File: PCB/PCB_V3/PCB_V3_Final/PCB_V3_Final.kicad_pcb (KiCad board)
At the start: 2 copper layers, 84 parts, among them J1 ESP_Left, J10 LHS_Arrow_+ve, J11 MCP_B0, J12 LHS_Arrow_-ve, J13 ACS2_Screw, J14 ACS4_Screw, J15 LAN8720_pins_2, J16 LAN8720_pins_1, J17 MCP_VCC_LINE, J18 RHS_Arrow_+ve, J19 RHS_Arrow_-ve, J2 ESP_Right, J20 AMS_IP_Pins, J21 BC1_IN+, J22 BC1_IN-, J23 BC3_IN+, J24 BC3_IN-, J25 AMS_OP_Pins, J26 BC1_OUT+, J27 BC1_OUT-, J28 BC3_OUT+, J29 BC3_OUT-, J3 ACS1_Pins, J30 STATIC_LED_1, J31 STATIC_LED_2, J32 BC2_IN+, J33 BC2_IN-, J34 BC5_IN+, J35 BC5_IN-, J36 I/P_Terminal, J37 Battery_Terminal, J38 BC2_OUT+, J39 BC2_OUT-, J4 ACS3_Pins, J40 BC5_OUT+, J41 BC5_OUT-, J5 ACS3_Screw, J6 ACS1_Screw, J7 ACS2_pins, J8 MCP_A0, J9 ACS4_Pins, Q1 IRLZ44N, Q10 IRLZ44N, Q2 IRLZ44N, Q3 IRLZ44N, Q4 IRLZ44N, Q5 IRLZ44N, Q6 IRLZ44N, Q7 IRLZ44N, Q8 IRLZ44N, Q9 IRLZ44N

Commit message: Uploading the final PCB files
1. Finished product
2. Made the remaining connections
3. Added the mounting holes for the PCB
4. Final producct --> has to be reviewed in the meeting
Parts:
- added H1: MountingScrew, MountingHole:MountingHole_3.2mm_M3, F.Cu at (219.8, 25.2)
- added H2: MountingScrew, MountingHole:MountingHole_3.2mm_M3, F.Cu at (74.5, 25.2)
- added H3: MountingScrew, MountingHole:MountingHole_3.2mm_M3, F.Cu at (75.5, 154.0)
- added H4: MountingScrew, MountingHole:MountingHole_3.2mm_M3, F.Cu at (219.2, 154.0)
- moved R23 98.9 mm to (92.2, 147.9)
- moved R24 96.5 mm to (102.3, 151.5), turned to 180 degrees
- moved Q10 41.0 mm to (130.3, 108.5)
- moved R15 41.0 mm to (135.8, 106.5)
- moved R20 41.0 mm to (145.9, 110.0)
- moved Q6 32.0 mm to (130.0, 143.5)
- moved R11 32.0 mm to (135.9, 143.5)
- moved R16 32.0 mm to (146.1, 147.0)
- moved Q9 22.5 mm to (130.0, 117.5)
- moved R14 22.5 mm to (135.4, 116.0)
- moved R19 22.5 mm to (145.6, 119.5)
- moved R26 15.9 mm to (131.5, 51.0), turned to 180 degrees
- moved Q7 14.0 mm to (129.8, 135.0)
- moved R12 14.0 mm to (135.8, 134.5)
- moved R17 14.0 mm to (145.9, 138.0)
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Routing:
- net /5V: track 0.00 -> 303.5 mm, vias 0 -> 2
- net /12V_LR: track 0.00 -> 295.6 mm, vias 0 -> 2
- net /LHS_LED_IP+: track 0.00 -> 259.6 mm
- net /RHS_LED_IP+: track 0.00 -> 256.6 mm
- net /D35: track 0.00 -> 169.7 mm, vias 0 -> 1
- net /D34: track 0.00 -> 162.4 mm
- net /D32: track 0.00 -> 155.0 mm
- net /BATT_VD: track 0.00 -> 137.5 mm, vias 0 -> 6
- net /D33: track 0.00 -> 133.4 mm
- net /14.5: track 15.1 -> 138.9 mm
- net /LHS_LED_1: track 0.00 -> 109.3 mm
- net /D13: track 12.6 -> 112.3 mm, vias 0 -> 4
- net /LHS_LED_2: track 0.00 -> 99.1 mm
- net /B0: track 0.00 -> 91.1 mm
- net /LHS_LED_3: track 0.00 -> 85.6 mm
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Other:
- board outline added: 152.5 x 136.2 mm
- board text added: "12V"
- board text added: "5V"
- board text added: "ACS712"
- board text added: "Battery_Terminal"
- board text added: "I/P_Terminal"
- board text added: "IN+"
- board text added: "LAN PORT HERE"
- board text added: "LHS_+ve"
- board text added: "LHS_-ve"
- board text added: "RHS_+ve"
- board text added: "RHS_-ve"
- board text added: "SCL"
- board text added: "SDA"
- board text added: "Static_LED_1"
- board text added: "Static_LED_2"
- board text added: "TOP"
- board text added: "VCC"
- board text added: "VOUT"

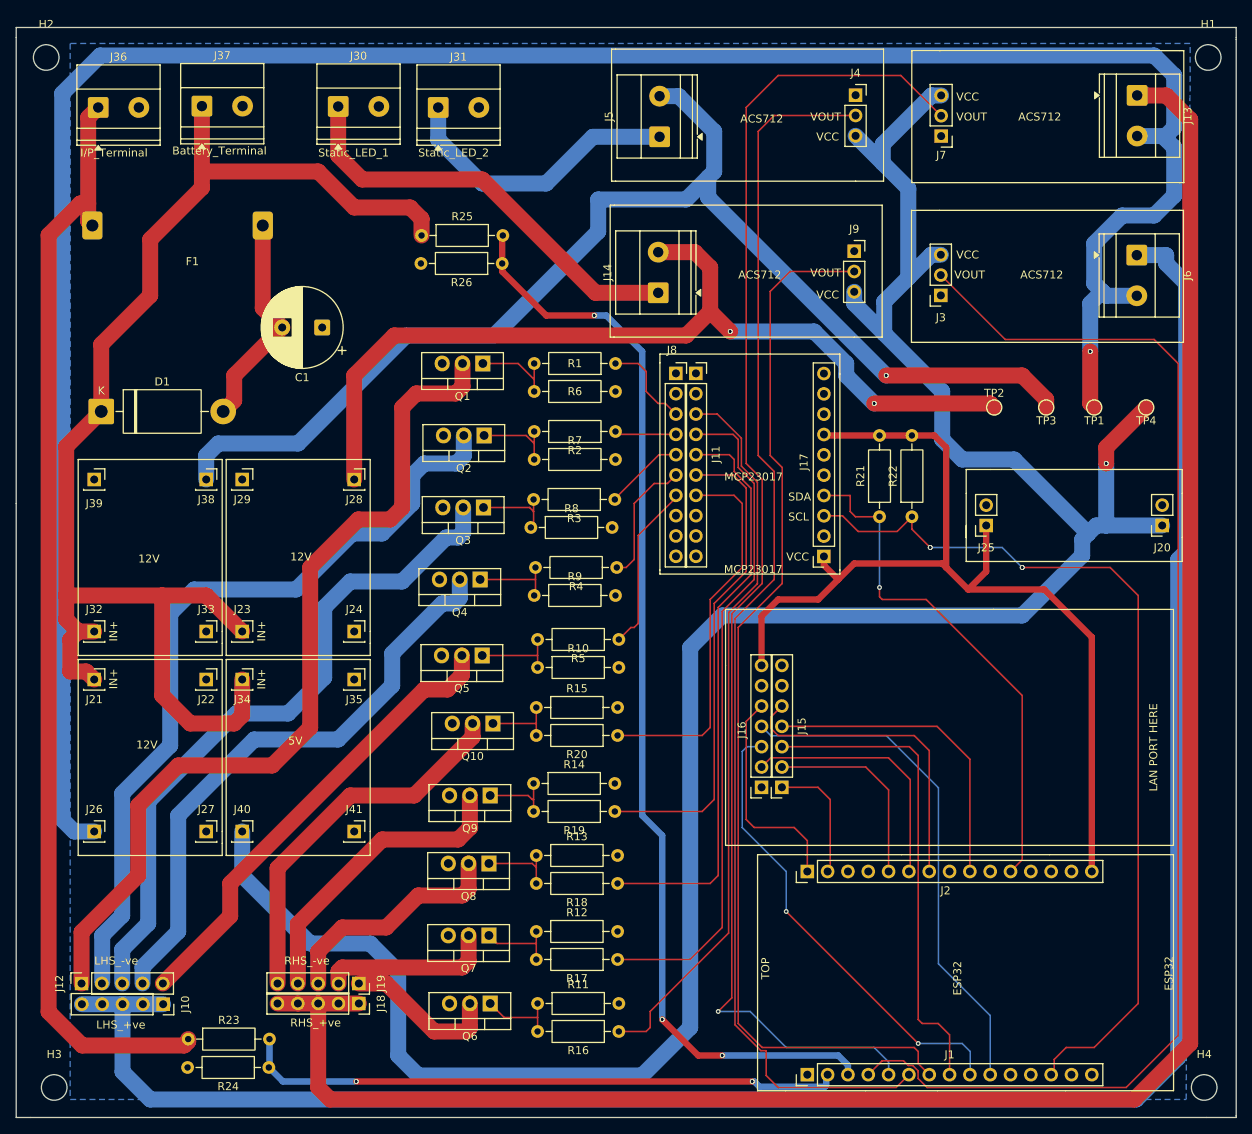
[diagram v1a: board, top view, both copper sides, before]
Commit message: Created and finished coding the firmware_test.ino file
1. Added a README file in the testing folder, that shows all the details of the hardware and software fucntionality
2. Created a test code for testing hardware first
3. Adding a testing criteria document for details of what is getting tested and how to test teh hardware using this code
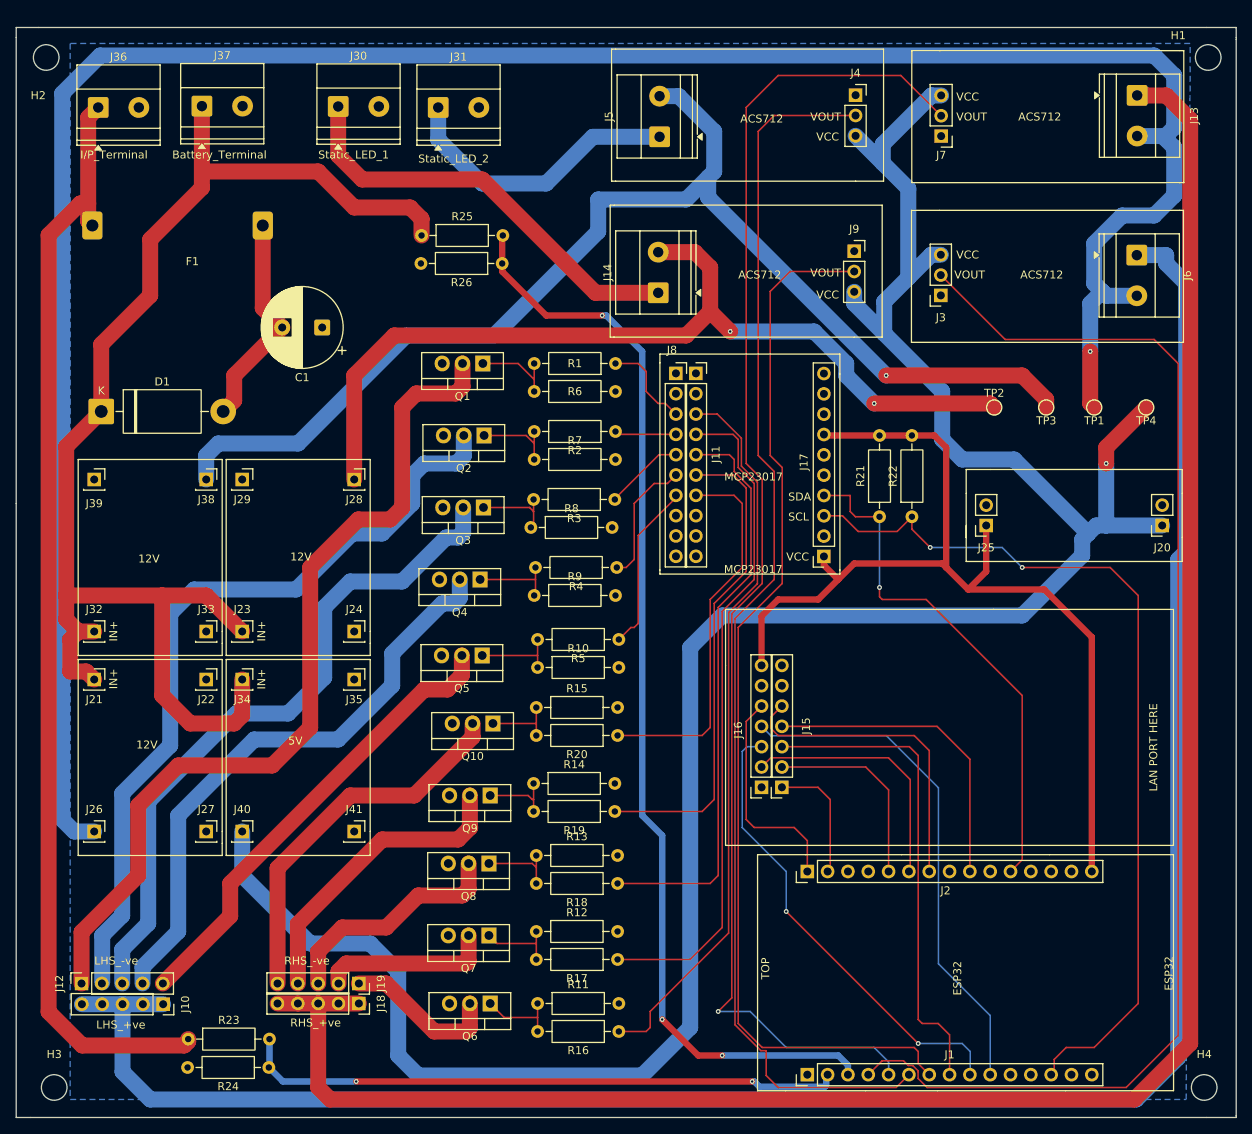
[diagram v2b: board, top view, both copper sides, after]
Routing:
- net /BATT_VD: vias 6 -> 3
- net /PSU_VD: vias 4 -> 2
- net /D13: vias 4 -> 2
- net /5V: vias 2 -> 1
- net /12V_STATIC2: vias 4 -> 2
- net /12V_STATIC1: vias 2 -> 1
- net /12V_LR: vias 2 -> 1
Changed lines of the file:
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@@
 		(tags "Through hole socket strip THT 1x07 2.54mm single row")
 		(property "Reference" "J16"
-			(at 2.46 7.16 90)
+			(at 2.92 7.16 90)
 			(layer "F.SilkS")
 			(effects
@@
 		(tags "mountinghole M3")
 		(property "Reference" "H1"
-			(at 0 -4.15 0)
+			(at -3.75 -2.75 0)
 			(layer "F.SilkS")
 			(effects
@@
 		(tags "Through hole socket strip THT 1x07 2.54mm single row")
 		(property "Reference" "J15"
-			(at -2.5 7.66 90)
+			(at -3.04 7.66 90)
 			(layer "F.SilkS")
 			(effects
@@
 		(tags "mountinghole M3")
 		(property "Reference" "H2"
-			(at 0 -4.15 0)
+			(at -1 4.75 0)
 			(layer "F.SilkS")
 			(effects
@@
 		(tags "THT Terminal Block Phoenix MKDS-1,5-2-5.08 pitch 5.08mm size 10.2x9.8mm drill 1.3mm pad 2.6mm")
 		(property "Reference" "J13"
-			(at 2.54 -6.32 90)
+			(at 2.54 -7.130715 90)
 			(layer "F.SilkS")
 			(effects
@@
 	)
 	(gr_text "I/P_Terminal\n"
-		(at 78.75 37.75 0)
+		(at 78.75 38 0)
 		(layer "F.SilkS")
 		(effects
@@
 	)
 	(gr_text "Battery_Terminal\n"
-		(at 90.25 37.5 0)
+		(at 90.25 38 0)
 		(layer "F.SilkS")
 		(effects
@@
 	)
 	(gr_text "Static_LED_1"
-		(at 108.5 37.75 0)
+		(at 108.5 38 0)
 		(layer "F.SilkS")
 		(effects
@@
 	)
 	(gr_text "Static_LED_2"
-		(at 121 37.75 0)
+		(at 121 38.5 0)
 		(layer "F.SilkS")
 		(effects
@@
 	(segment
 		(start 111.04 139.46)
-		(end 111.5 139)
+		(end 112 138.5)
 		(width 2)
 		(layer "F.Cu")
@@
 	)
 	(segment
-		(start 127.3 138.2)
-		(end 127.3 135)
+		(start 111.04 141)
+		(end 111.04 139.46)
 		(width 2)
 		(layer "F.Cu")
@@
 	)
 	(segment
-		(start 126.5 139)
-		(end 127.3 138.2)
+		(start 127.3 138.2)
+		(end 127.3 135)
 		(width 2)
 		(layer "F.Cu")
@@
 	)
 	(segment
-		(start 111.5 139)
-		(end 126.5 139)
+		(start 127 138.5)
+		(end 127.3 138.2)
 		(width 2)
 		(layer "F.Cu")
@@
 	)
 	(segment
-		(start 111.04 141)
-		(end 111.04 139.46)
+		(start 112 138.5)
+		(end 127 138.5)
 		(width 2)
 		(layer "F.Cu")
@@
 	)
 	(via
-		(at 160 59.5)
-		(size 0.6)
-		(drill 0.3)
-		(layers "F.Cu" "B.Cu")
-		(net "/12V_STATIC2")
-	)
-	(via
-		(at 178 68.5)
-		(size 0.6)
-		(drill 0.3)
-		(layers "F.Cu" "B.Cu")
-		(net "/12V_STATIC2")
-	)
-	(via
 		(at 178 68.5)
 		(size 0.6)
@@
 		(net "/PSU_VD")
 	)
-	(via
-		(at 113.25 153.25)
-		(size 0.6)
-		(drill 0.3)
-		(layers "F.Cu" "B.Cu")
-		(net "/PSU_VD")
-	)
-	(via
-		(at 162.75 153.25)
-		(size 0.6)
-		(drill 0.3)
-		(layers "F.Cu" "B.Cu")
-		(net "/PSU_VD")
-	)
 	(segment
 		(start 163 153.25)
@@
 	)
 	(segment
-		(start 131.5 51)
-		(end 131.5 52)
-		(width 0.8)
+		(start 131.5 47.58)
+		(end 131.58 47.5)
+		(width 0.2)
 		(layer "F.Cu")
 		(net "/BATT_VD")
 	)
 	(segment
-		(start 137 57.5)
-		(end 143 57.5)
+		(start 144 57.5)
+		(end 137 57.5)
 		(width 0.8)
 		(layer "F.Cu")
@@
 	)
 	(segment
-		(start 131.5 47.58)
-		(end 131.58 47.5)
-		(width 0.2)
+		(start 131.5 52)
+		(end 131.5 51)
+		(width 0.8)
 		(layer "F.Cu")
 		(net "/BATT_VD")
@@
 	)
 	(segment
-		(start 131.5 52)
-		(end 137 57.5)
+		(start 131.5 51)
+		(end 131.5 47.58)
 		(width 0.8)
 		(layer "F.Cu")
@@
 	)
 	(segment
-		(start 131.5 51)
-		(end 131.5 47.58)
+		(start 137 57.5)
+		(end 131.5 52)
 		(width 0.8)
 		(layer "F.Cu")
@@
 	)
 	(via
-		(at 143 57.5)
-		(size 0.6)
-		(drill 0.3)
-		(layers "F.Cu" "B.Cu")
-		(net "/BATT_VD")
-	)
-	(via
-		(at 143 57.5)
+		(at 144 57.5)
 		(size 0.6)
 		(drill 0.3)
@@
 		(net "/BATT_VD")
 	)
-	(via
-		(at 159 150)
-		(size 0.6)
-		(drill 0.3)
-		(layers "F.Cu" "B.Cu")
+	(segment
+		(start 149 62)
+		(end 149 120)
+		(width 0.8)
+		(layer "B.Cu")
 		(net "/BATT_VD")
 	)
-	(via
-		(at 151.5 145.5)
-		(size 0.6)
-		(drill 0.3)
-		(layers "F.Cu" "B.Cu")
+	(segment
+		(start 144 57.5)
+		(end 144.5 57.5)
+		(width 0.8)
+		(layer "B.Cu")
 		(net "/BATT_VD")
 	)
@@
 	)
 	(segment
-		(start 143 57.5)
-		(end 144.5 57.5)
-		(width 0.8)
-		(layer "B.Cu")
-		(net "/BATT_VD")
-	)
-	(segment
 		(start 173.5 150)
 		(end 174.72 151.22)
@@
 	)
 	(segment
-		(start 144.5 57.5)
-		(end 149 62)
-		(width 0.8)
-		(layer "B.Cu")
-		(net "/BATT_VD")
-	)
-	(segment
 		(start 174.72 151.22)
 		(end 174.72 152.4)
@@
 	)
 	(segment
-		(start 149 62)
-		(end 149 120)
+		(start 144.5 57.5)
+		(end 149 62)
 		(width 0.8)
 		(layer "B.Cu")
@@
 		(net "/D13")
 	)
-	(via
-		(at 185 86.5)
-		(size 0.6)
-		(drill 0.3)
-		(layers "F.Cu" "B.Cu")
-		(net "/D13")
-	)
-	(via
-		(at 196.5 89)
-		(size 0.6)
-		(drill 0.3)
-		(layers "F.Cu" "B.Cu")
-		(net "/D13")
-	)
 	(segment
 		(start 185 86.5)
@@
 		(net "/12V_STATIC1")
 	)
-	(via
-		(at 179.5 65)
-		(size 0.6)
-		(drill 0.3)
-		(layers "F.Cu" "B.Cu")
-		(net "/12V_STATIC1")
-	)
 	(segment
 		(start 158 34.5)
@@
 		(net "/12V_LR")
 	)
-	(via
-		(at 205 62)
-		(size 0.6)
-		(drill 0.3)
-		(layers "F.Cu" "B.Cu")
-		(net "/12V_LR")
-	)
 	(segment
 		(start 215.5 42.5)
@@
 		(net "/5V")
 	)
-	(via
-		(at 207 76)
-		(size 0.6)
-		(drill 0.3)
-		(layers "F.Cu" "B.Cu")
-		(net "/5V")
-	)
 	(segment
 		(start 99 127.5)
@@
 	)
 	(segment
-		(start 158.5 94)
-		(end 158.5 127.5)
+		(start 162.6 79.1)
+		(end 162.6 89.9)
 		(width 0.2)
 		(layer "F.Cu")
@@
 	)
 	(segment
+		(start 158.5 94)
+		(end 158.5 127.5)
+		(width 0.2)
+		(layer "F.Cu")
+		(net "/B2")
+	)
+	(segment
 		(start 158.5 127.5)
 		(end 157.5 128.5)
@@
 	)
 	(segment
-		(start 157.5 128.5)
-		(end 145.92 128.5)
+		(start 155.714285 74.900001)
+		(end 159.900001 74.900001)
 		(width 0.2)
 		(layer "F.Cu")
@@
 	)
 	(segment
-		(start 160.5 75.5)
-		(end 160.5 77)
+		(start 157.5 128.5)
+		(end 145.92 128.5)
 		(width 0.2)
 		(layer "F.Cu")
@@
 	)
 	(segment
-		(start 155.714285 74.900001)
-		(end 159.900001 74.900001)
-		(width 0.2)
-		(layer "F.Cu")
-		(net "/B2")
-	)
-	(segment
-		(start 162.6 79.1)
-		(end 162.6 89.9)
+		(start 160.5 75.5)
+		(end 160.5 77)
 		(width 0.2)
 		(layer "F.Cu")

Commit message: Final PCB Upload
1. Made all the changes
2. final PCB files and the gerber files uploaded
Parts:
- D1: value 1N5822 -> D_Schottky; footprint Diode_THT:D_DO-201AD_P15.24mm_Horizontal -> Package_TO_SOT_THT:TO-220-2_Vertical
- J28: value BC3_OUT+ -> BC3_IN-
- moved D1 8.77 mm to (89.9, 67.5)
- moved C1 5.00 mm to (104.0, 59.0), turned to 0 degrees
- moved J10 0.09 mm to (89.1, 143.5)
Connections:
- C1 pad 1: GND -> /14.5_VD
- C1 pad 2: Net-(D1-A) -> GND
- D1 pad 2: Net-(D1-A) -> /14.5_VD
- F1 pad 2: Net-(D1-A) -> /14.5_VD
- J23 pad 1: /MAIN_OP -> /12V_STATIC2
- J28 pad 1: /12V_STATIC2 -> GND
- J29 pad 1: GND -> /MAIN_OP
- J32 pad 1: /MAIN_OP -> /12V_STATIC1
- J38 pad 1: /12V_STATIC1 -> GND
- J39 pad 1: GND -> /MAIN_OP
- R23 pad 1: /14.5 -> /14.5_VD
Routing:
- net /14.5_VD: track 0.00 -> 168.1 mm, vias 0 -> 2
- net /14.5: track 138.9 -> 15.5 mm
- net /12V_STATIC1: track 153.4 -> 182.6 mm
- net Net-(D1-A): track 27.3 -> 0.00 mm
- net /12V_STATIC2: track 115.0 -> 141.2 mm
- net /MAIN_OP: track 168.9 -> 189.4 mm
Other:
- board text added: "100"
- board text added: "100k"
- board text added: "10k"
- board text added: "18k"
- board text added: "3v3"
- board text added: "4.7k"
- board text added: "470u"
- board text added: "A0/B0"
- board text added: "A1/B1"
- board text added: "A2/B2"
- board text added: "A3/B3"
- board text added: "A4/B4"
- board text added: "Fuse_Holder"
- board text added: "GND"
- board text added: "IN-"
- board text added: "IP+"
- board text added: "LR_Arrows 12V"
- board text added: "OP+"
- board text added: "OUT+"
- board text added: "OUT-"
- board text added: "RESET"
- board text added: "S D G"
- board text added: "Static_LED_1 12V"
- board text added: "Static_LED_2 12V"

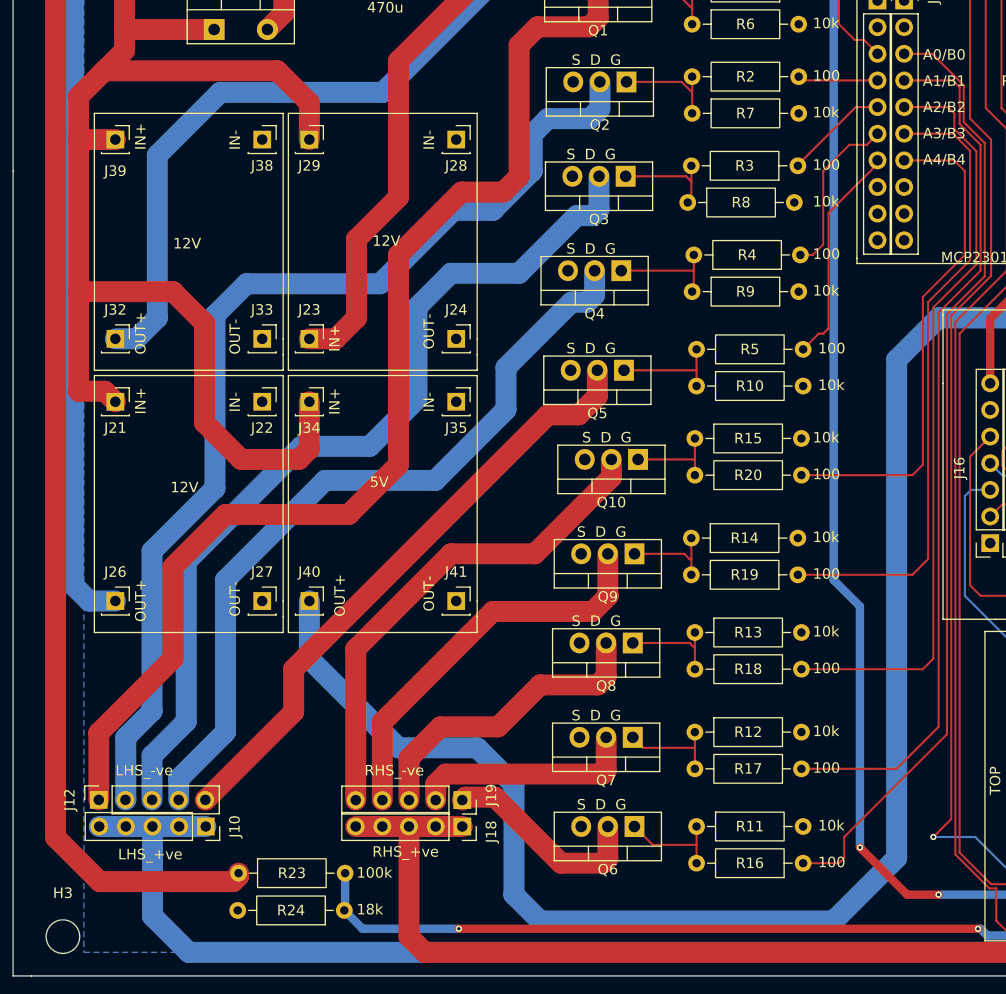
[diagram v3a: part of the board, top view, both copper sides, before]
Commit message: Updated the PCB
1. Updated the PCB spacing for the buck converter modules
2. Made a separate folder for the gerber v2

This is the final gerber and PCB files
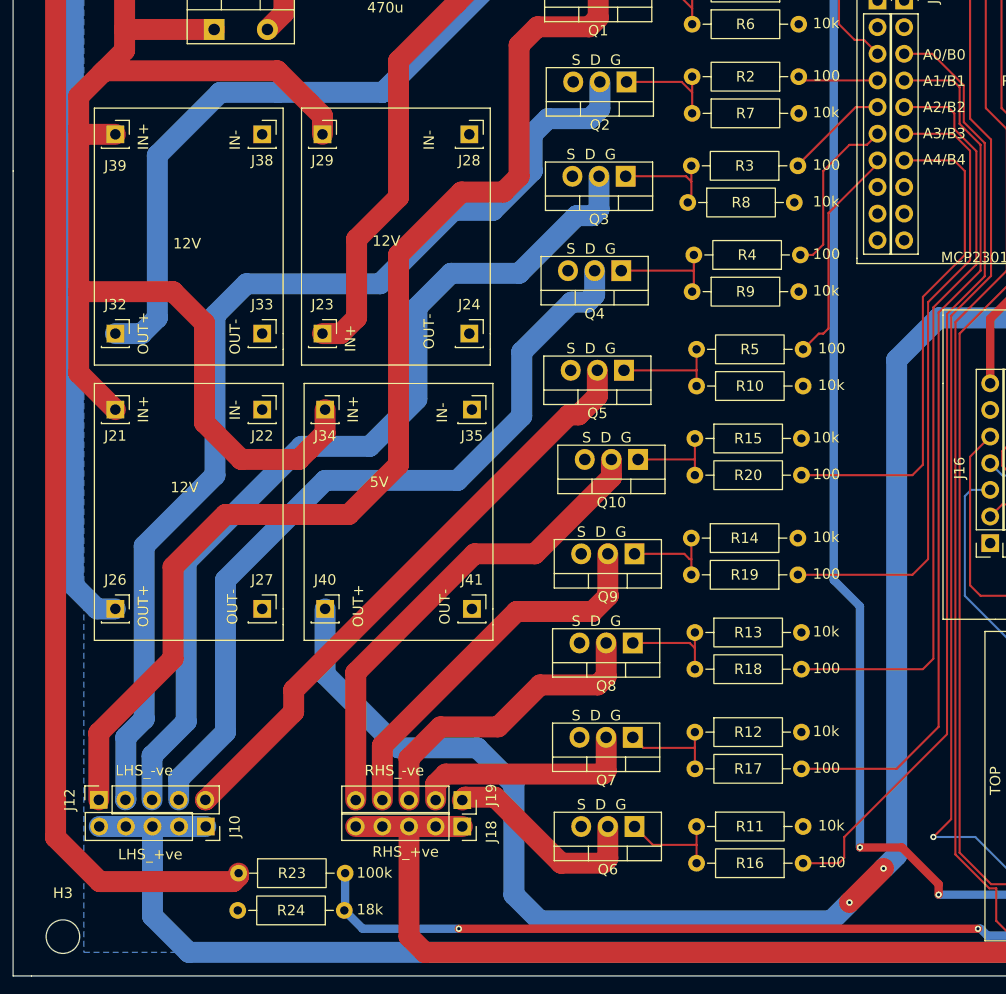
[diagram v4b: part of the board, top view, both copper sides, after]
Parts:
- moved J34 1.68 mm to (100.5, 103.8)
- moved J35 1.68 mm to (114.5, 103.8)
- moved J40 1.68 mm to (100.5, 122.8)
- moved J41 1.68 mm to (114.5, 122.8)
- moved J23 1.35 mm to (100.2, 96.5)
- moved J24 1.35 mm to (114.2, 96.5)
- moved J28 1.35 mm to (114.2, 77.5)
- moved J29 1.35 mm to (100.2, 77.5)
- moved J21 0.75 mm to (80.5, 103.8)
- moved J22 0.75 mm to (94.5, 103.8)
- moved J26 0.75 mm to (80.5, 122.8)
- moved J27 0.75 mm to (94.5, 122.8)
- moved J32 0.50 mm to (80.5, 96.5)
- moved J33 0.50 mm to (94.5, 96.5)
- moved J38 0.50 mm to (94.5, 77.5)
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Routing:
- net /5V: track 303.5 -> 302.0 mm, vias 1 -> 3
- net /12V_STATIC2: track 141.2 -> 139.8 mm
- net /MAIN_OP: track 189.4 -> 188.1 mm
- net /RHS_LED_5: track 47.3 -> 45.9 mm
- net /RHS_LED_4: track 38.0 -> 36.7 mm
- net /LHS_LED_4: track 73.9 -> 75.2 mm
- net /LHS_LED_5: track 58.2 -> 57.0 mm
- net /BATT_VD: track 137.5 -> 138.1 mm
